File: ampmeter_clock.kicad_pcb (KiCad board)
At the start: 4 copper layers, 148 parts, among them J1 Barrel_Jack_Switch, Q1 2N7002, Q10 2N7002, Q11 2N7002, Q12 2N7002, Q13 2N7002, Q14 2N7002, Q15 2N7002, Q16 2N7002, Q17 2N7002, Q18 2N7002, Q19 2N7002, Q2 2N7002, Q20 NCE30P12S, Q3 2N7002, Q4 2N7002, Q5 2N7002, Q6 2N7002, Q7 2N7002, Q8 2N7002, Q9 2N7002, SW1 SET_MIN, SW2 SET_HOUR, SW3 RESET, SW4 CLK_HALT, U1 4027, U10 4516, U11 4516, U2 40106, U3 40106, U4 4081, U5 4081, U6 4060, U7 4510, U8 4516, U9 4510, Y1 32.768kHz

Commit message: PCB done
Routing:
- net Net-(U11-Pad7): track 18.9 -> 156.4 mm, vias 0 -> 4
- net ~CI_STAGE3: track 31.1 -> 156.9 mm, vias 3 -> 8
- net HOUR_3: track 27.2 -> 148.6 mm, vias 2 -> 7
- net Net-(U1-Pad10): track 0.00 -> 119.4 mm, vias 0 -> 5
- net Net-(U10-Pad5): track 0.00 -> 117.4 mm, vias 0 -> 3
- net HOUR_4: track 16.2 -> 123.6 mm, vias 2 -> 7
- net RST_STAGE3: track 0.00 -> 105.5 mm, vias 0 -> 3
- net RST: track 81.0 -> 184.0 mm, vias 4 -> 6
- net CLK: track 115.3 -> 207.8 mm, vias 8 -> 12
- net MIN_5: track 14.2 -> 106.3 mm, vias 2 -> 6
- net SEC_5: track 14.2 -> 99.9 mm, vias 2 -> 6
- net Net-(U2-Pad1): track 0.00 -> 79.5 mm, vias 0 -> 2
- net MIN_6: track 34.1 -> 111.3 mm, vias 3 -> 6
- net Net-(D6-Pad1): track 7.96 -> 83.9 mm, vias 2 -> 7
- net ~CI_STAGE2: track 34.4 -> 107.6 mm, vias 3 -> 6
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- added copper zone on B.Cu, net GND
- added copper zone on F.Cu, net GND
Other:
- board text added: "Ampmeter Clock"
- board text added: "Rev.1"
- board text added: "www.sleepyponylabs.com"

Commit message: Fix PCB Edge, add ibom
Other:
- board outline added: 100 x 100 mm
- board text added: "JLCJLCJLCJLC"

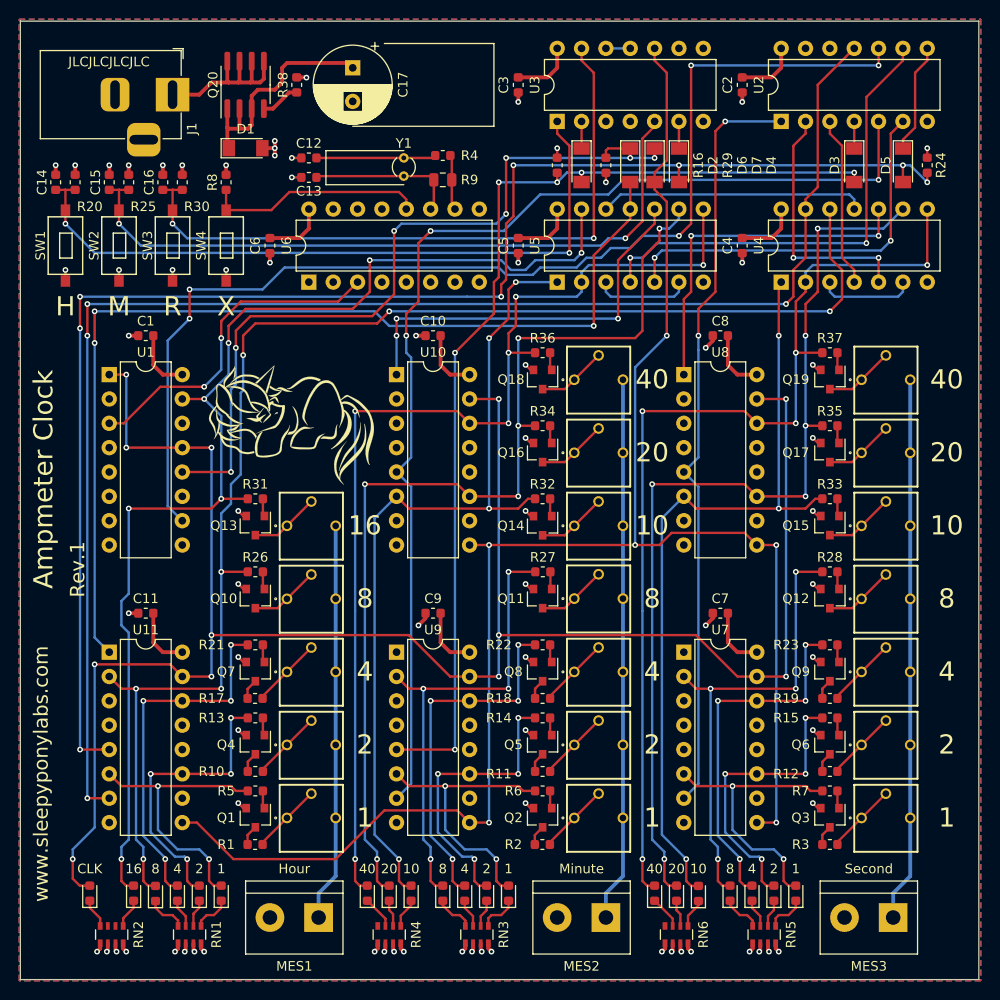
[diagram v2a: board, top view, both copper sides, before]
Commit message: Fix swapped H and M buttons and misc traces adjustments
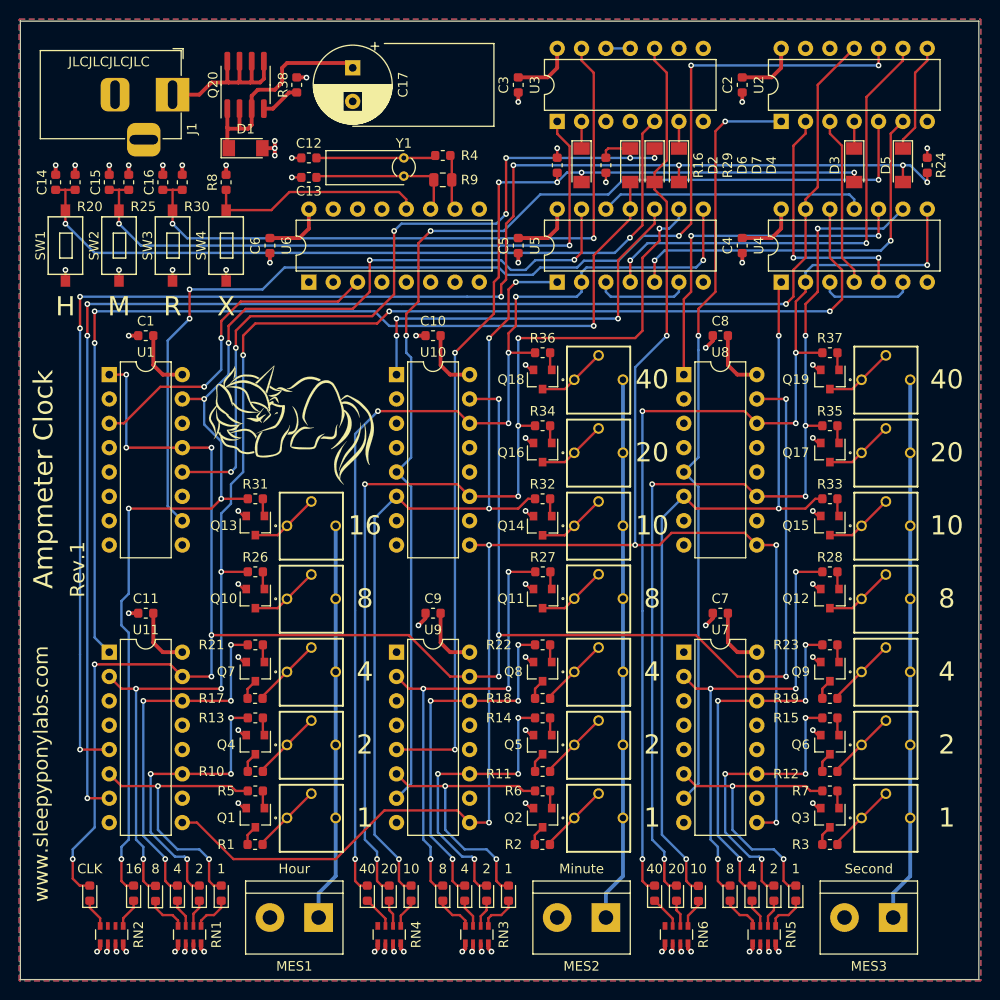
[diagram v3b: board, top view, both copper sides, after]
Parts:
- SW1: value SET_MIN -> SET_HOUR
- SW2: value SET_HOUR -> SET_MIN
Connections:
- U3 pad 1: Net-(C14-Pad1) -> Net-(C15-Pad1)
- U3 pad 5: Net-(C15-Pad1) -> Net-(C14-Pad1)
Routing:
- net Net-(C15-Pad1): track 73.1 -> 67.0 mm
- net Net-(C14-Pad1): track 73.7 -> 79.6 mm
- net MIN_6: track 111.3 -> 109.6 mm

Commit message: Fix silk, generate ibom for rev 2
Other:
- board text added: "Ammeter Clock"
- board text added: "Rev.2"
- board text removed: "Ampmeter Clock"
- board text removed: "Rev.1"
